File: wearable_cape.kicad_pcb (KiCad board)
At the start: 2 copper layers, 70.5 x 54.6 mm, 72 parts, among them J1 JACK_3P, J2 JACK_3P, J3 JACK_3P, P1 BELA_AINS, P2 RECEIVER, P3 BATTERY, P4 BELA_AOUTS, P5 PWR_OUT, SW1 SW_HALT, SW2 SW_MODE_SEL, U1 MCP6004, U2 MCP6004, U3 BEAGLEBONEBLACK, U4 OKI_7805

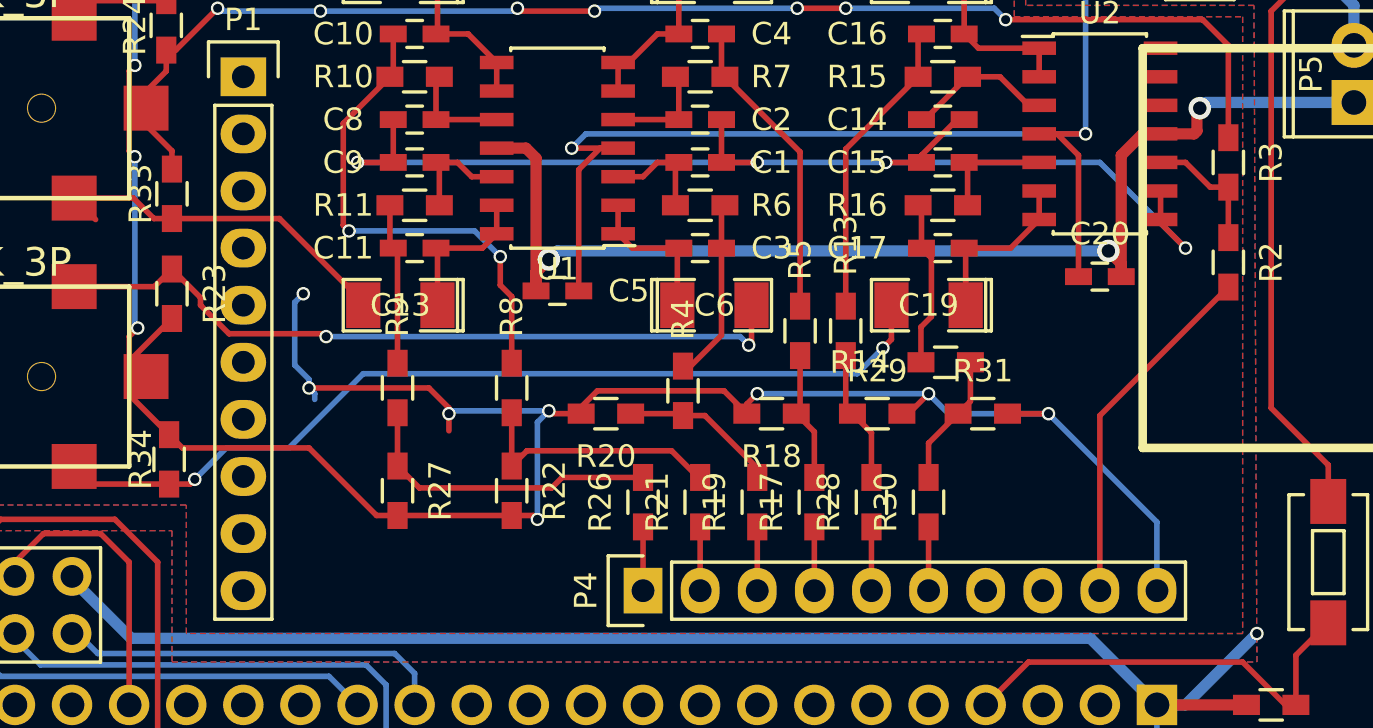
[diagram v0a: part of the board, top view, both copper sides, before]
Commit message: add ferrite beads, and fix GNDA -> 1.8_VREF
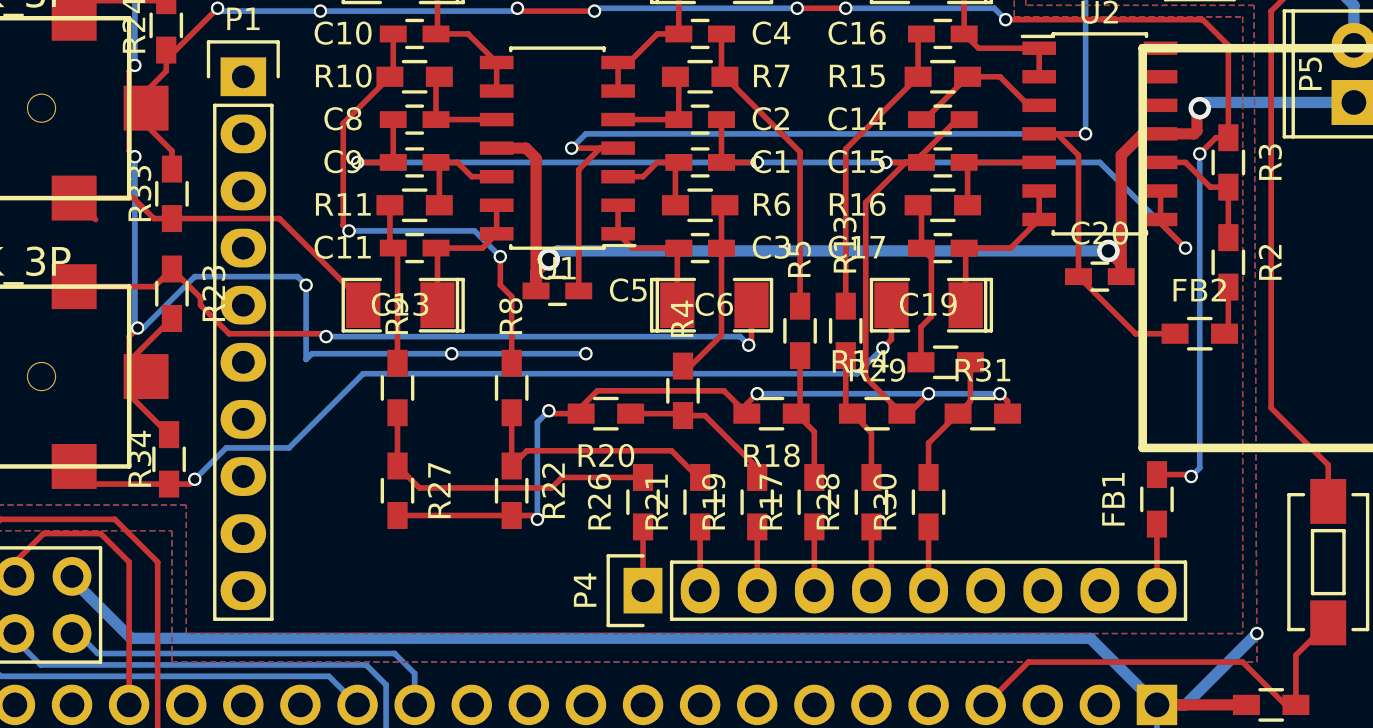
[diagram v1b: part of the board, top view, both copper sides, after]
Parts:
- added FB1: FILTER, Resistors_SMD:R_0603_HandSoldering, F.Cu at (90.2, 59.4)
- added FB2: FILTER, Resistors_SMD:R_0603_HandSoldering, F.Cu at (92.1, 52.1)
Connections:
- P4 pad 10: GNDA -> Net-(FB1-Pad1)
- P4 pad 9: VCC -> Net-(P4-Pad9)
- R18 pad 2: GNDA -> REF_1.8V
- R20 pad 2: GNDA -> REF_1.8V
- R22 pad 2: GNDA -> REF_1.8V
- R27 pad 2: GNDA -> REF_1.8V
- R29 pad 2: GNDA -> REF_1.8V
- R31 pad 2: GNDA -> REF_1.8V
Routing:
- net REF_1.8V: track 52.9 -> 101.8 mm, vias 4 -> 9
- net GNDA: track 175.5 -> 139.8 mm, vias 19 -> 16
- net VCC: track 15.9 -> 2.15 mm
- net SYS_5V: track 67.0 -> 72.4 mm
- net Net-(FB1-Pad1): track 0.00 -> 2.96 mm

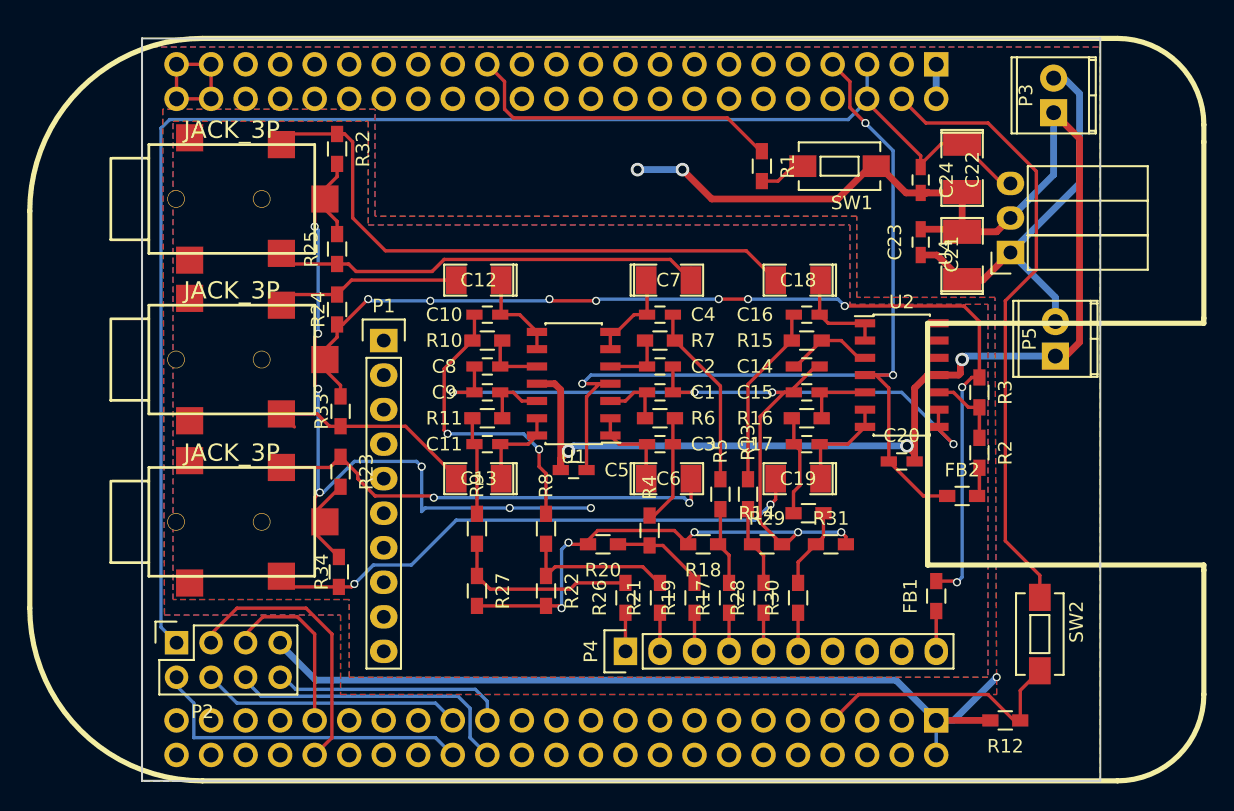
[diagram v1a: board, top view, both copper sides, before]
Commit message: updates: footprint check, cutout for regulator, larger power input screw terminal
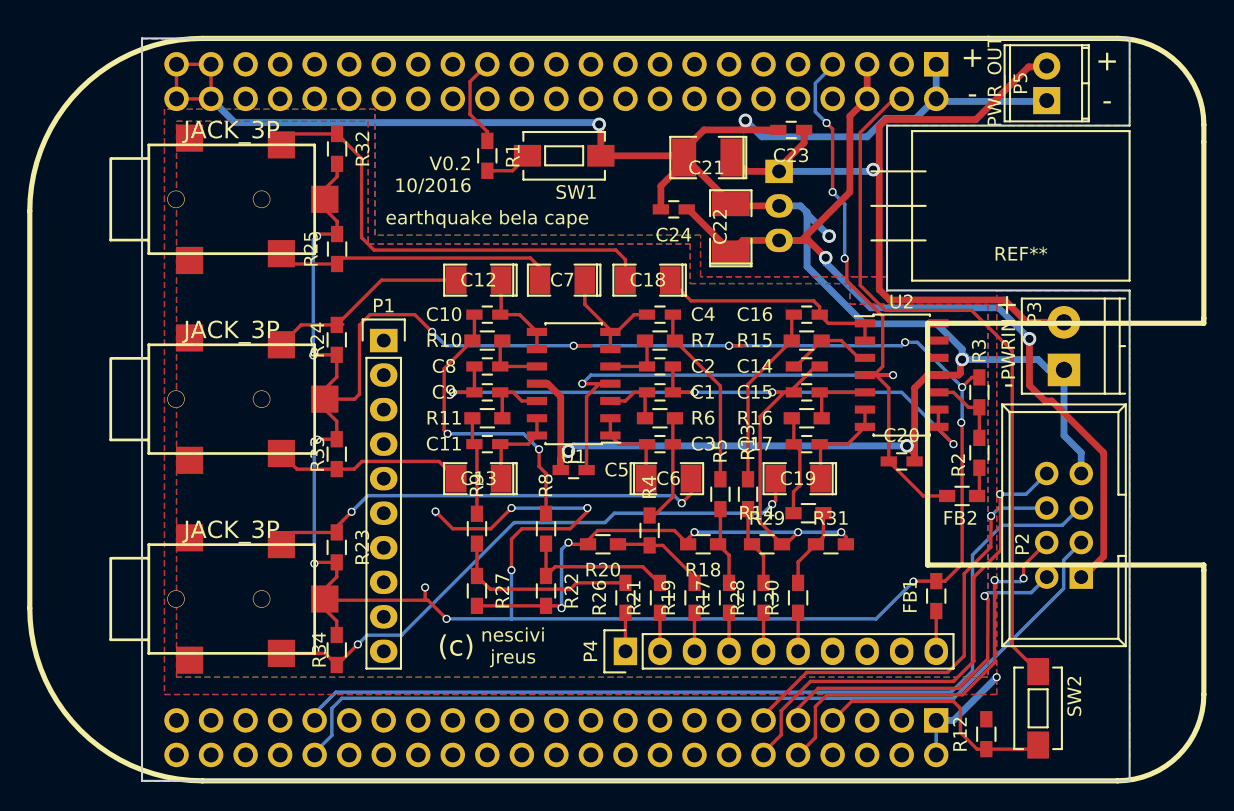
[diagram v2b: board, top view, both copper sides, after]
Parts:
- added REF**: OKI_outline, OKI_outline, F.Cu at (96.4, 30.7)
- P2: footprint Socket_Strips:Socket_Strip_Straight_2x04 -> IDC_header_8pin:IDC_Header_Straight_10pins
- P3: value BATTERY -> BATT; footprint Terminal_Blocks:TerminalBlock_Pheonix_MPT-2.54mm_2pol -> Terminal_Blocks:TerminalBlock_Pheonix_PT-3.5mm_2pol
- U4: moved to B.Cu
- moved P2 66.7 mm to (100.8, 58.0), turned to 90 degrees
- moved SW1 20.3 mm to (62.8, 27.1)
- moved R1 20.2 mm to (57.1, 27.1)
- moved C21 20.0 mm to (73.4, 27.2), turned to 180 degrees
- moved P3 18.9 mm to (99.6, 42.8)
- moved P5 18.8 mm to (98.3, 23.0)
- moved C24 18.3 mm to (70.9, 31.0), turned to 180 degrees
- moved U4 18.0 mm to (78.6, 28.2), turned to 270 degrees
- moved C22 17.6 mm to (75.1, 32.4), turned to 90 degrees
- moved C23 12.6 mm to (79.5, 25.1), turned to 180 degrees
- moved C18 11.0 mm to (69.0, 36.2)
- moved C7 7.81 mm to (62.7, 36.2), turned to 180 degrees
- moved R34 5.74 mm to (46.1, 63.4)
- moved J1 5.68 mm to (38.4, 59.6)
- moved R23 5.57 mm to (46.1, 55.9)
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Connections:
- P2 pad 2: /D15 -> /D2
- P2 pad 4: /D14 -> /D3
- P2 pad 6: /D13 -> /D4
- P2 pad 8: /D12 -> /D5
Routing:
- net /TX: track 13.1 -> 68.2 mm
- net GNDA: track 139.8 -> 194.3 mm, vias 16 -> 17
- net /RX: track 20.5 -> 65.3 mm
- net RAW_5V: track 109.1 -> 68.4 mm, vias 0 -> 2
- net /D5: track 0.00 -> 36.6 mm, vias 0 -> 1
- net /D4: track 0.00 -> 32.4 mm, vias 0 -> 1
- net /D3: track 0.00 -> 30.3 mm, vias 0 -> 2
- net /D2: track 0.00 -> 26.2 mm, vias 0 -> 1
- net BAT_11.1V: track 30.8 -> 55.6 mm, vias 0 -> 1
- net /D15: track 24.5 -> 0.00 mm
- net /D13: track 21.6 -> 0.00 mm
- net /D14: track 19.1 -> 0.00 mm
- net /D12: track 17.4 -> 0.00 mm
- net /~HALT: track 24.0 -> 6.68 mm
- net /FILT_OUT1: track 33.7 -> 21.0 mm
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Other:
- board size 70.5 x 54.6 mm -> 72.6 x 54.6 mm
- board text added: "(c)"
- board text added: "+"
- board text added: "-"
- board text added: "PWRIN"
- board text added: "V0.2 10/2016"
- board text added: "earthquake bela cape"
- board text added: "nescivi jreus"

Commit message: added several options for attenuation of circuit.
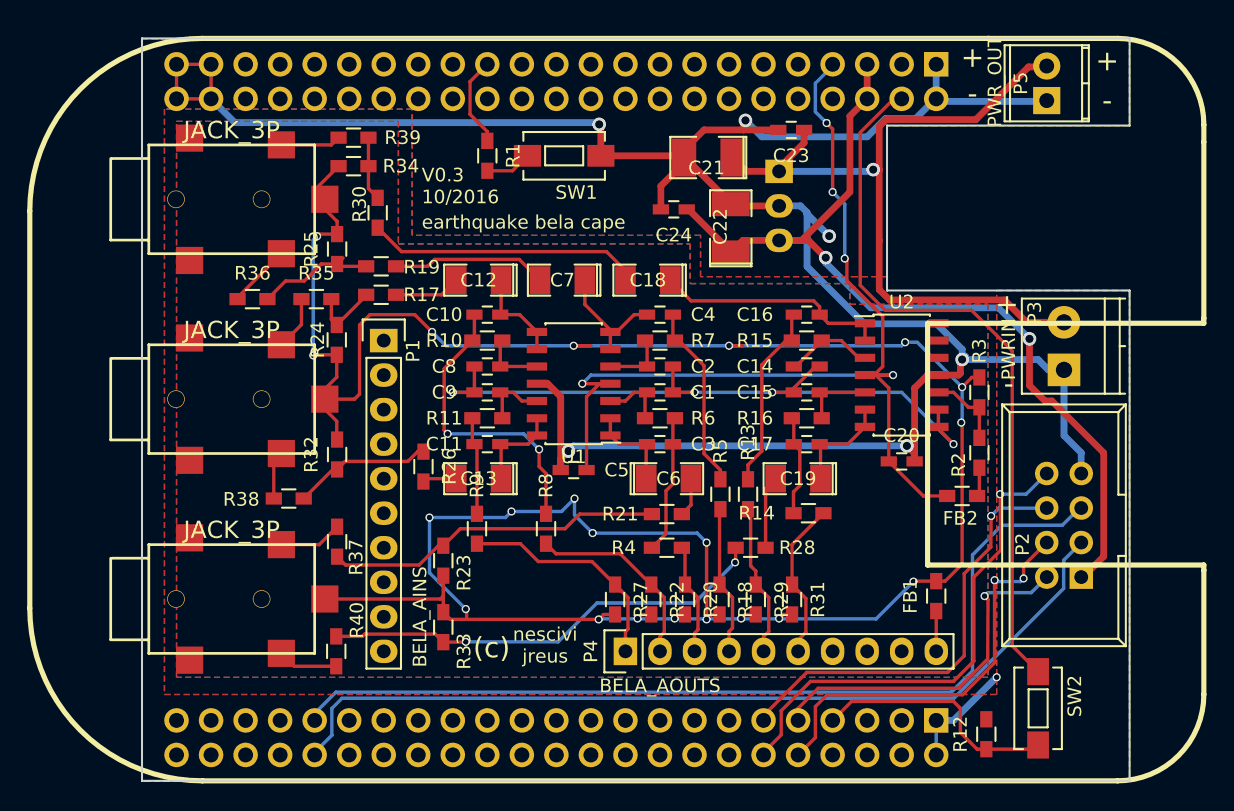
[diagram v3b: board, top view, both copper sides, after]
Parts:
- removed REF**: OKI_outline, OKI_outline
- added R35: 12k, Resistors_SMD:R_0603_HandSoldering, F.Cu at (44.6, 37.6)
- added R36: 12k, Resistors_SMD:R_0603_HandSoldering, F.Cu at (39.9, 37.6)
- added R37: 12k, Resistors_SMD:R_0603_HandSoldering, F.Cu at (46.1, 55.4)
- added R38: 12k, Resistors_SMD:R_0603_HandSoldering, F.Cu at (42.5, 52.3)
- added R39: 12k, Resistors_SMD:R_0603_HandSoldering, F.Cu at (47.3, 25.7)
- added R40: 12k, Resistors_SMD:R_0603_HandSoldering, F.Cu at (46.0, 63.5)
- P3: value BATT -> BATTERY
- R17, R19, R21, R26, R28, R30: value 150k -> 2k2
- R18, R20, R22, R27, R29, R31: value 200k -> 390
- R23, R24, R25, R32, R33, R34: value 100k -> 3k9
- moved R30 41.9 mm to (49.1, 31.2), turned to 270 degrees
- moved R34 35.6 mm to (47.3, 27.8), turned to 180 degrees
- moved R17 33.9 mm to (49.3, 37.3), turned to 180 degrees
- moved R19 33.6 mm to (49.3, 35.2), turned to 0 degrees
- moved R32 22.5 mm to (46.1, 49.0), turned to 90 degrees
- moved R26 17.7 mm to (52.5, 49.9), turned to 270 degrees
- moved R33 14.9 mm to (53.9, 61.7)
- moved R27 10.2 mm to (66.5, 59.7)
- moved R23 7.90 mm to (53.9, 56.8)
- moved R22 7.77 mm to (69.2, 59.7)
- moved R20 7.27 mm to (71.7, 59.7), turned to 270 degrees
- moved R21 6.18 mm to (70.4, 53.4), turned to 0 degrees
- moved R31 4.97 mm to (79.6, 59.7), turned to 270 degrees
- moved R18 4.24 mm to (74.2, 59.7), turned to 270 degrees
- moved R29 4.15 mm to (76.9, 59.7), turned to 270 degrees
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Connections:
- C12 pad 2: /FILT_OUT2 -> Net-(C12-Pad2)
- C13 pad 2: /FILT_OUT3 -> Net-(C13-Pad2)
- C18 pad 2: /FILT_OUT4 -> Net-(C18-Pad2)
- C19 pad 2: /FILT_OUT5 -> Net-(C19-Pad2)
- C6 pad 2: /FILT_OUT0 -> Net-(C6-Pad2)
- C7 pad 2: /FILT_OUT1 -> Net-(C7-Pad2)
- R13 pad 2: Net-(R13-Pad2) -> /BELA_OUT4
- R14 pad 2: Net-(R14-Pad2) -> /BELA_OUT5
- R17 pad 1: /BELA_OUT3 -> Net-(C12-Pad2)
- R18 pad 1: Net-(R17-Pad2) -> /BELA_OUT3
- R18 pad 2: REF_1.8V -> GNDA
- R19 pad 1: /BELA_OUT2 -> Net-(R19-Pad1)
- R19 pad 2: Net-(R19-Pad2) -> Net-(C7-Pad2)
- R20 pad 1: Net-(R19-Pad2) -> /BELA_OUT2
- R20 pad 2: REF_1.8V -> GNDA
- R21 pad 1: /BELA_OUT1 -> Net-(R21-Pad1)
- R21 pad 2: Net-(R21-Pad2) -> Net-(C6-Pad2)
- R22 pad 1: Net-(R21-Pad2) -> /BELA_OUT1
- R22 pad 2: REF_1.8V -> GNDA
- R23 pad 1: /FILT_OUT0 -> Net-(R21-Pad1)
- R24 pad 1: /FILT_OUT2 -> Net-(R17-Pad2)
- R25 pad 1: /FILT_OUT1 -> Net-(R19-Pad1)
- R26 pad 1: /BELA_OUT0 -> Net-(R26-Pad1)
- R26 pad 2: Net-(R26-Pad2) -> Net-(C13-Pad2)
- R27 pad 1: Net-(R26-Pad2) -> /BELA_OUT0
- R27 pad 2: REF_1.8V -> GNDA
- R28 pad 1: /BELA_OUT4 -> Net-(R28-Pad1)
- R28 pad 2: Net-(R13-Pad2) -> Net-(C19-Pad2)
- R29 pad 1: Net-(R13-Pad2) -> /BELA_OUT4
- R29 pad 2: REF_1.8V -> GNDA
- R30 pad 1: /BELA_OUT5 -> Net-(R30-Pad1)
- R30 pad 2: Net-(R14-Pad2) -> Net-(C18-Pad2)
- R31 pad 1: Net-(R14-Pad2) -> /BELA_OUT5
- R31 pad 2: REF_1.8V -> GNDA
- R32 pad 1: /FILT_OUT4 -> Net-(R26-Pad1)
- R33 pad 1: /FILT_OUT3 -> Net-(R28-Pad1)
- R34 pad 1: /FILT_OUT5 -> Net-(R30-Pad1)
- R4 pad 2: Net-(R19-Pad2) -> /BELA_OUT2
- R5 pad 2: Net-(R17-Pad2) -> /BELA_OUT3
- R8 pad 2: Net-(R21-Pad2) -> /BELA_OUT1
- R9 pad 2: Net-(R26-Pad2) -> /BELA_OUT0
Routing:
- net REF_1.8V: track 101.8 -> 52.9 mm, vias 9 -> 4
- net /FILT_OUT5: track 43.5 -> 4.43 mm, vias 2 -> 0
- net Net-(R28-Pad1): track 0.00 -> 33.2 mm, vias 0 -> 2
- net /FILT_OUT4: track 34.4 -> 5.54 mm
- net /FILT_OUT0: track 33.5 -> 5.91 mm, vias 2 -> 0
- net Net-(R21-Pad1): track 0.00 -> 25.3 mm
- net Net-(C18-Pad2): track 0.00 -> 20.2 mm
- net /FILT_OUT1: track 21.0 -> 6.05 mm
- net /BELA_OUT0: track 2.84 -> 16.8 mm
- net Net-(R26-Pad2): track 13.9 -> 0.00 mm
- net /BELA_OUT1: track 2.84 -> 14.4 mm
- net Net-(R21-Pad2): track 11.5 -> 0.00 mm
- net Net-(C7-Pad2): track 0.00 -> 11.4 mm
- net /FILT_OUT2: track 15.3 -> 3.97 mm
- net /FILT_OUT3: track 14.6 -> 3.54 mm
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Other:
- board text added: "V0.3 10/2016"
- board text removed: "V0.2 10/2016"

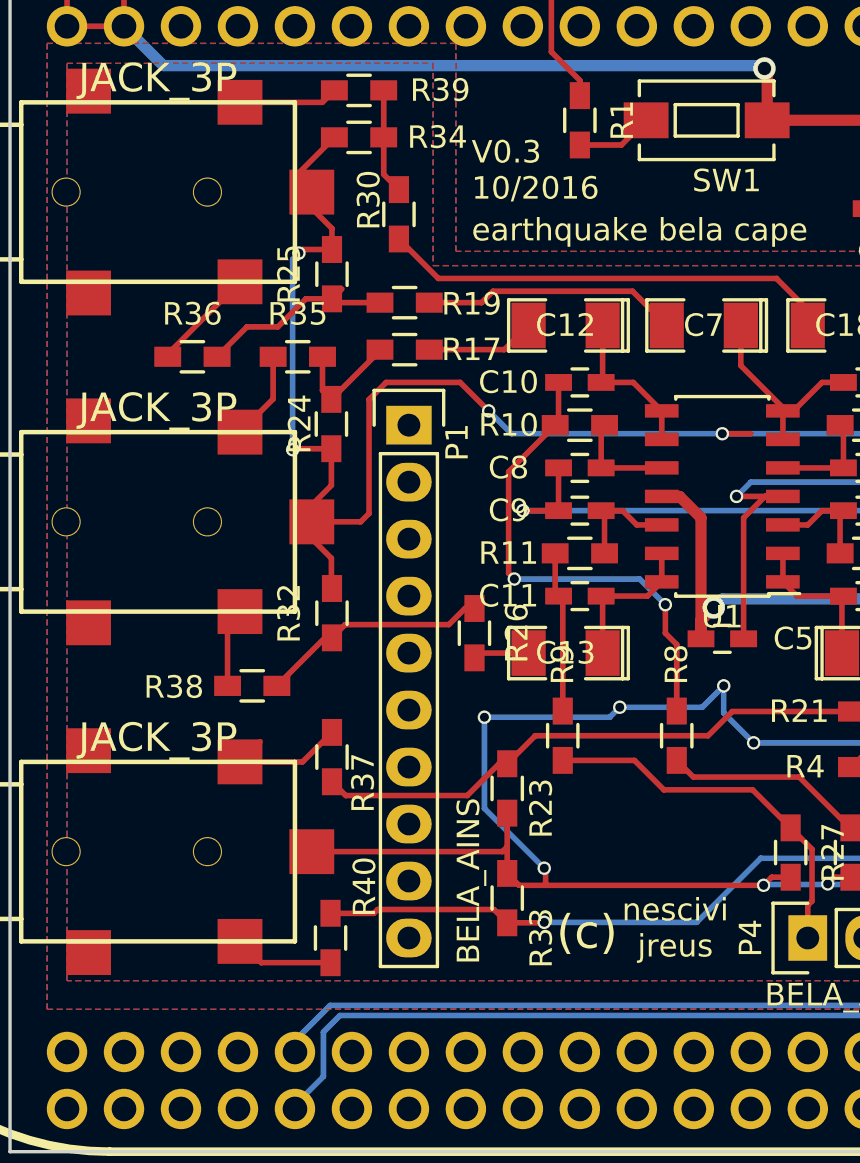
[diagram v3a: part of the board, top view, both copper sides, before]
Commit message: fixed jack plugs pinout and made numbering of outputs consistent.
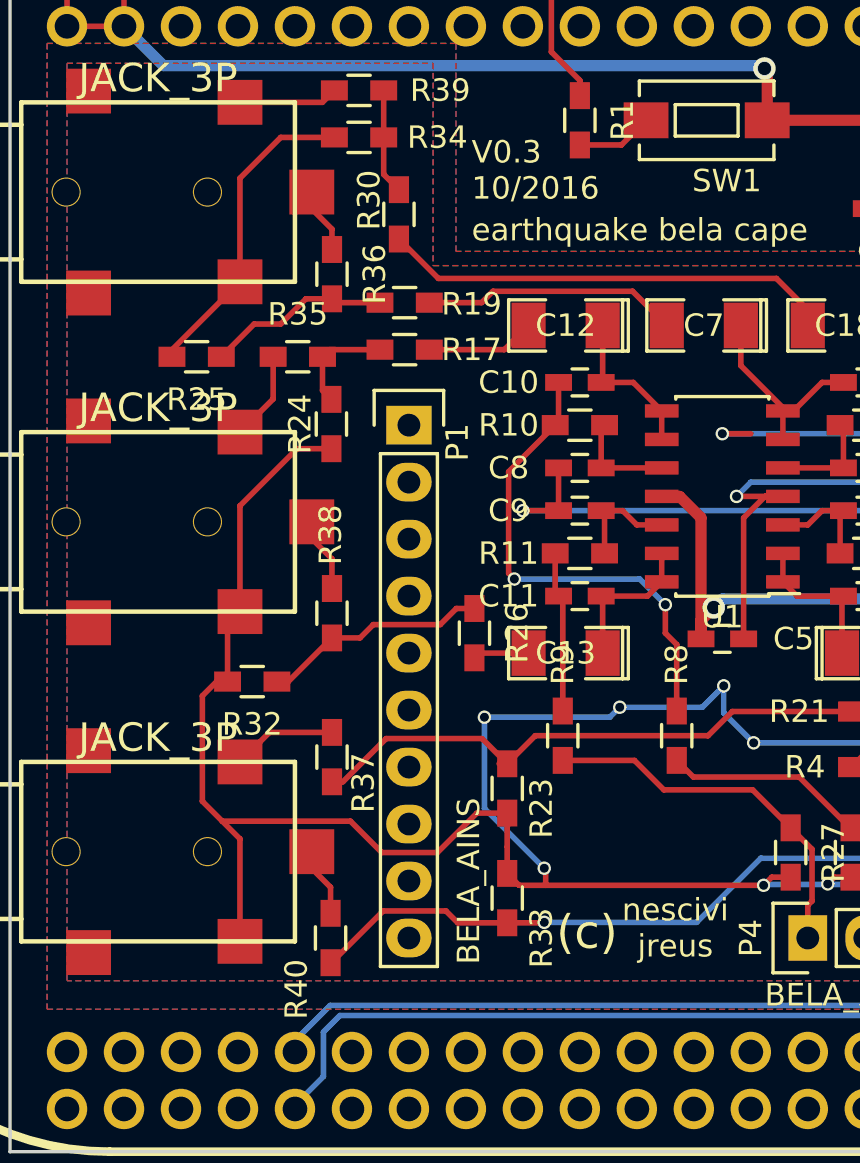
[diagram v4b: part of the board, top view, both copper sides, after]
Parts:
- moved R36 7.23 mm to (46.1, 33.9), turned to 270 degrees
- moved R25 7.07 mm to (40.1, 37.6), turned to 180 degrees
- moved R38 4.81 mm to (46.1, 49.0), turned to 270 degrees
- moved R32 4.68 mm to (42.5, 52.1), turned to 180 degrees
- turned R40 to 270 degrees
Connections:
- net /FILT_OUT0 renamed /A_FILT_OUT2
- net /FILT_OUT2 renamed /A_FILT_OUT1
- net /FILT_OUT4 renamed /A_FILT_OUT4
- J1 pad 1: /FILT_OUT5 -> GNDA
- J1 pad 2: GNDA -> /A_FILT_OUT5
- J2 pad 1: /FILT_OUT3 -> GNDA
- J2 pad 2: GNDA -> /A_FILT_OUT0
- J3 pad 1: /FILT_OUT1 -> GNDA
- J3 pad 2: GNDA -> /A_FILT_OUT3
- R36 pad 1: /FILT_OUT1 -> /A_FILT_OUT3
- R38 pad 1: /FILT_OUT3 -> /A_FILT_OUT0
- R40 pad 1: /FILT_OUT5 -> /A_FILT_OUT5
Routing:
- net /FILT_OUT1: track 6.05 -> 0.00 mm
- net /A_FILT_OUT3: track 0.00 -> 4.83 mm
- net GNDA: track 196.1 -> 191.3 mm, vias 21 -> 18
- net /FILT_OUT5: track 4.43 -> 0.00 mm
- net /A_FILT_OUT0: track 0.00 -> 3.66 mm
- net /FILT_OUT3: track 3.54 -> 0.00 mm
- net /A_FILT_OUT5: track 0.00 -> 3.54 mm
- net Net-(R28-Pad1): track 33.2 -> 34.0 mm
- net Net-(R21-Pad1): track 25.3 -> 26.1 mm
- net Net-(R19-Pad1): track 9.02 -> 8.45 mm
